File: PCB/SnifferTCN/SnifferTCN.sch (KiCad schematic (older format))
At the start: 180 parts, among them IC101 IC Reg 3,3 V AP3512EMPTR-G1, J101 VBATG, J102 VBAT+, J103 12 VOLTS, J104 Protoboard GPIO 1, J105 5 VOLTS, J106 Conector RJ45, J107 3,3 VOLTS, J108 Protoboard GPIO 2, J109 Conector USB_B 2, J110 Conector USB_B 1, J111 Conector USB Vertical, J112 Conector 12 V/GND x 2, J113 Debug/Serial, J114 JTAG uP, J115 Micro_SD_Card, J116 Conector RS485 x 6, J117 Conector RS485 x 3, J118 DB9 Hembra, J119 DB9 Macho, J121 JTAG MVB, SW101 RESET, SW102 Pulsador 1, SW103 RESET_MVB, SW104 SWITCH MVB, SW105 Pulsador 2, U101 IC uP STM32H743ZIT6, U102 SN74LVCR162245DGGR, U103 SN74AVC16827DGVR, U104 MVBC02D, U105 IC Ethernet KSZ8081RNA, U106 IC USBLC6-2SC6, U107 IC USBLC6-2SC6, U108 IC USBLC6-2SC6, U109 MIC2005A, U110 S25FL127SABMFI101, U112 IC Debug/Serial, U113 IC TM CY7C1051DV33-10ZSXI, U114 IC RS485 ISL83485IBZ, U115 IC RS485 ISL83485IBZ, U116 IC RS485 ISL83485IBZ, U117 IC RS485 ISL83485IBZ, U118 IC RS485 ISL83485IBZ, U119 IC Reg 5 V AP63205WU-7, Y101 8MHz, Y102 32.768KHz, Y103 25MHz, Y104 XT 24 MHz

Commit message: Ethernet WIP
Lib y Footprint descargados del nuevo diseño.
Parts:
- removed D101, D102: B120-E3, Diode_SMD:D_SOD-123, symbol Diode:B120-E3
- added C132, C134: 1u, Capacitor_SMD:C_0805_2012Metric, symbol Device:C_Small
- added C151, C152: 120u, Capacitor_SMD:C_0805_2012Metric, symbol Device:C_Small
- added R154, R155: 10KR, Resistor_SMD:R_0805_2012Metric, symbol Device:R_Small
- added U111, U120: MIC2005A, Package_TO_SOT_SMD:SOT-23-5, symbol SnifferTCN-rescue:MIC2005A-mic20xx
- C126: value 2.2u -> 1u; manf# CL21B225KPFNNNE -> (none)
- C127: value 2.2u -> 120u; manf# CL21B225KPFNNNE -> (none)
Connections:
- net +3V3: now also R154.1, R155.1
- net +5V: now also C132.1, C134.1, U111.1 (VIN), U120.1 (VIN)
- net ENABLE_USB: now also U111.3 (ENABLE), U120.3 (ENABLE)
- net ERR_USB: now also R154.2, R155.2, U111.4 (~FAUKT), U120.4 (~FAUKT)
- net GND: now also C132.2, C134.2, C151.2, C152.2, U111.2 (GND), U120.2 (GND)
- net VBUS1: now also C151.1, U111.5 (VOUT)
- net VBUS2: now also C152.1, U120.5 (VOUT)
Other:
- note added: "SerialUSB"
- note added: "USB OTG FS"
- note added: "USB OTG HS"
- moved on the sheet: C126, C127, J109, J110, J111, R137, U106, U107, U108, U109

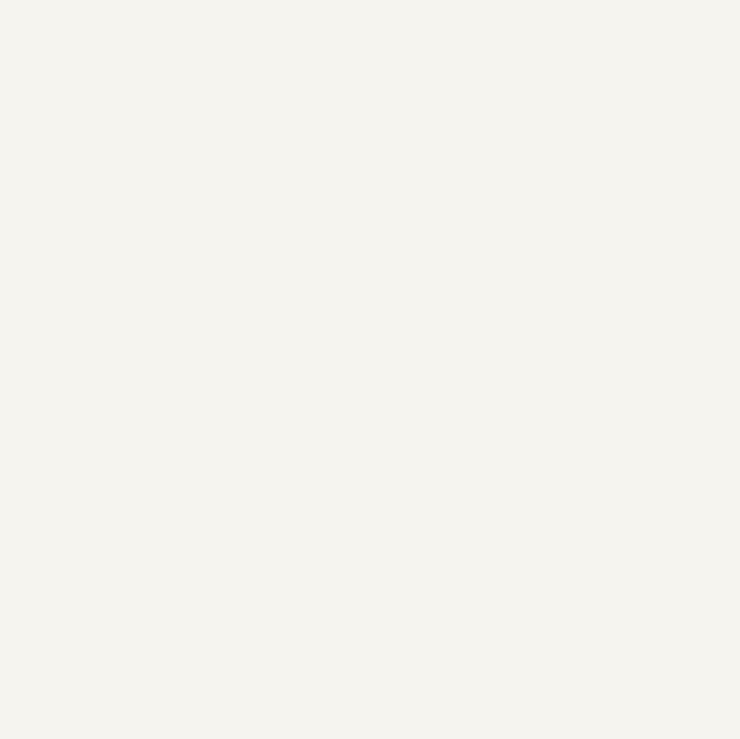
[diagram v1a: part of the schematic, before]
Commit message: Compra Componentes
Se actualizo listado componentes debido a faltantes por COVID.
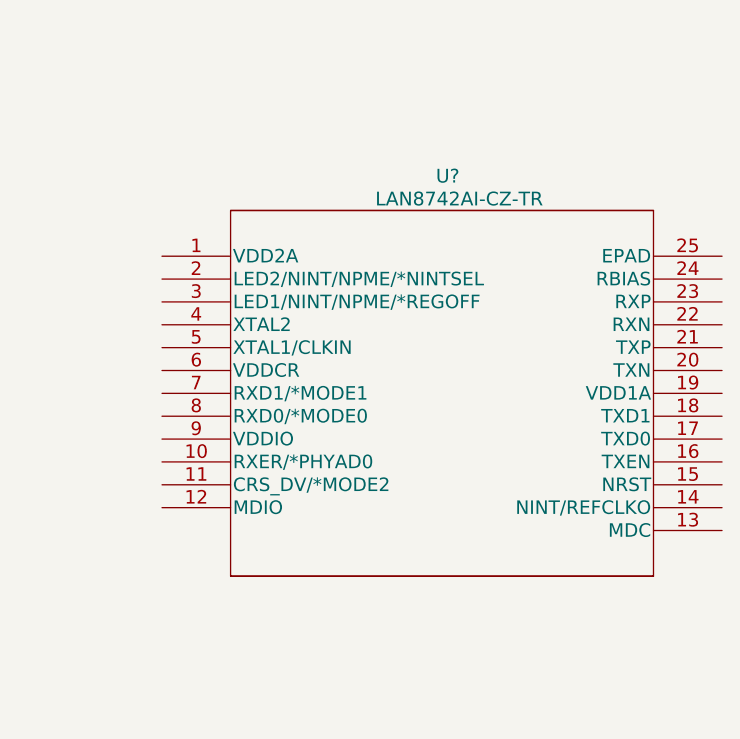
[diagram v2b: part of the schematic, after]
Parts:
- added U?: LAN8742AI-CZ-TR, SQFN24_4X4MC_MCH, symbol LAN8742AICZTR_Sequential:LAN8742AI-CZ-TR
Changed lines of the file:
@@
 Wire Wire Line
 	20300 5050 20700 5050
+$Comp
+L LAN8742AICZTR_Sequential:LAN8742AI-CZ-TR U?
+U 1 1 5F9EF593
+P 28700 15150
+F 0 "U?" H 29950 15500 60  0000 C CNN
+F 1 "LAN8742AI-CZ-TR" H 30000 15400 60  0000 C CNN
+F 2 "SQFN24_4X4MC_MCH" H 31000 15390 60  0001 C CNN
+F 3 "" H 28700 15150 60  0000 C CNN
+	1    28700 15150
+	1    0    0    -1
+$EndComp
 $EndSCHEMATC

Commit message: Reforma New Components
Reforma por componentes nuevos/distintos debido a falta de stock en DigiKey (dos reguladores e IC LAN)
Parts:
- removed C148: 0.1u, Capacitor_SMD:C_0805_2012Metric, symbol Device:C_Small
- removed C149, C150: 2.2u, Capacitor_SMD:C_0805_2012Metric, symbol Device:C_Small
- removed U119: IC Reg 5 V AP63205WU-7, SOIC_05WU-7_DIO, symbol AP63205WU-7:AP63205WU-7
- removed U?: LAN8742AI-CZ-TR, SQFN24_4X4MC_MCH, symbol LAN8742AICZTR_Sequential:LAN8742AI-CZ-TR
- added C153: 10u, Capacitor_SMD:C_0805_2012Metric, symbol Device:C_Small
- added C157: 470n, Capacitor_SMD:C_0805_2012Metric, symbol Device:C_Small
- added C158: 68n, Capacitor_SMD:C_0805_2012Metric, symbol Device:C_Small
- added C159: 10n, Capacitor_SMD:C_0805_2012Metric, symbol Device:C_Small
- added C160: 2.2p, Capacitor_SMD:C_0805_2012Metric, symbol Device:C_Small
- added C161: 330p, Capacitor_SMD:C_0805_2012Metric, symbol Device:C_Small
- added C162: 20u, Capacitor_SMD:C_0805_2012Metric, symbol Device:C_Small
- added IC102: L6986H5V, SOP65P640X120-17N, symbol SnifferTCN-rescue:L6986H5V-L6986H5V
- added R156: 1K, Resistor_SMD:R_0805_2012Metric, symbol Device:R_Small
- added R157: 75K, Resistor_SMD:R_0805_2012Metric, symbol Device:R_Small
- added R158: 240K, Resistor_SMD:R_0805_2012Metric, symbol Device:R_Small
- added R159: 82K, Resistor_SMD:R_0805_2012Metric, symbol Device:R_Small
- added U?: KSZ8091MNXIA-TR, QFN-32_MCH, symbol KSZ8091MNXIA-TR:KSZ8091MNXIA-TR
- C147: value 10u -> 1u
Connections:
- net +12V: now also C153.1, IC102.15 (VIN)
- net +5V: now also C162.2, IC102.16 (VBIAS), R156.2, R158.1
- net GND: no longer C128.2, C147.2, C155.2, C156.2, J112.2 (Pin_2)
- net at L102.1: now also IC102.13 (LX_1), IC102.14 (LX_2)
- new net: IC102.1 (RST), R156.1
- new net: C157.1, IC102.2 (VCC), IC102.6 (MLF)
- new net: C158.1, IC102.3 (SS/~INH)
- new net: C160.1, IC102.7 (COMP), R157.1
- new net: C159.1, IC102.8 (DELAY)
- new net: IC102.9 (FB/VOUT), R158.2, R159.1
- new net: C161.2, R157.2
- new net GNDPWR: C128.2, C147.2, C153.2, C155.2, C156.2, C157.2, C158.2, C159.2, C160.2, C161.1, C162.1, IC102.10 (SGND), IC102.11 (PGND_1), IC102.12 (PGND_2), IC102.17 (EP), IC102.5 (FSW), J112.2 (Pin_2), R159.2
- no-connect marks 14 -> 15
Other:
- note removed: "POWER 5 V"
- moved on the sheet: C147, L102
